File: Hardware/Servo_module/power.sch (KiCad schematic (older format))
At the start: 11 parts, among them P2 CONN_2, P3 CONN_2

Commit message: [HARDWARE][SERVO_MODULE] Schematic
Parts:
- R2: value 1k -> 820
- R3: value 330 -> 220
- R4: value 560 -> 330
- gave numbers to parts that had none: 1
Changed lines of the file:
@@
-EESchema Schematic File Version 2  date Fri 18 Oct 2013 03:55:12 PM CEST
+EESchema Schematic File Version 2
 LIBS:power
 LIBS:device
@@
 LIBS:conn_2_jst
 LIBS:conn_4_jst
+LIBS:sn65hvd232d
 LIBS:serv_module-cache
-EELAYER 24  0
+EELAYER 27 0
 EELAYER END
-$Descr A4 11700 8267
+$Descr A4 11693 8268
+encoding utf-8
 Sheet 2 4
 Title ""
-Date "18 oct 2013"
+Date "25 oct 2013"
 Rev ""
 Comp ""
@@
 	5000 5450 5200 5450
 $Comp
-L LED D?
+L LED D3
 U 1 1 52613CD7
 P 5200 5250
-F 0 "D?" H 5200 5350 50  0000 C CNN
+F 0 "D3" H 5200 5350 50  0000 C CNN
 F 1 "LED" H 5200 5150 50  0000 C CNN
+F 2 "" H 5200 5250 60  0001 C CNN
+F 3 "" H 5200 5250 60  0001 C CNN
 	1    5200 5250
 	0    1    1    0
@@
 P 5200 4750
 F 0 "R4" V 5280 4750 50  0000 C CNN
-F 1 "560" V 5200 4750 50  0000 C CNN
+F 1 "330" V 5200 4750 50  0000 C CNN
+F 2 "" H 5200 4750 60  0001 C CNN
+F 3 "" H 5200 4750 60  0001 C CNN
 	1    5200 4750
 	-1   0    0    1
@@
 F 0 "#PWR?" H 7350 3700 30  0001 C CNN
 F 1 "GND" H 7350 3630 30  0001 C CNN
+F 2 "" H 7350 3700 60  0001 C CNN
+F 3 "" H 7350 3700 60  0001 C CNN
 	1    7350 3700
 	1    0    0    -1
@@
 F 0 "D2" H 7350 3550 50  0000 C CNN
 F 1 "LED" H 7350 3350 50  0000 C CNN
+F 2 "" H 7350 3450 60  0001 C CNN
+F 3 "" H 7350 3450 60  0001 C CNN
 	1    7350 3450
 	0    1    1    0
@@
 P 7050 3250
 F 0 "R3" V 7130 3250 50  0000 C CNN
-F 1 "330" V 7050 3250 50  0000 C CNN
+F 1 "220" V 7050 3250 50  0000 C CNN
+F 2 "" H 7050 3250 60  0001 C CNN
+F 3 "" H 7050 3250 60  0001 C CNN
 	1    7050 3250
 	0    1    1    0
@@
 F 0 "#PWR?" H 4800 2350 30  0001 C CNN
 F 1 "GND" H 4800 2280 30  0001 C CNN
+F 2 "" H 4800 2350 60  0001 C CNN
+F 3 "" H 4800 2350 60  0001 C CNN
 	1    4800 2350
 	1    0    0    -1
@@
 F 0 "D1" H 4950 2600 50  0000 C CNN
 F 1 "LED" H 4950 2400 50  0000 C CNN
+F 2 "" H 4950 2500 60  0001 C CNN
+F 3 "" H 4950 2500 60  0001 C CNN
 	1    4950 2500
 	0    -1   -1   0
@@
 P 4950 3000
 F 0 "R2" V 5030 3000 50  0000 C CNN
-F 1 "1k" V 4950 3000 50  0000 C CNN
+F 1 "820" V 4950 3000 50  0000 C CNN
+F 2 "" H 4950 3000 60  0001 C CNN
+F 3 "" H 4950 3000 60  0001 C CNN
 	1    4950 3000
 	1    0    0    -1
@@
 F 0 "#PWR?" H 5100 5500 30  0001 C CNN
 F 1 "GND" H 5100 5430 30  0001 C CNN
+F 2 "" H 5100 5500 60  0001 C CNN
+F 3 "" H 5100 5500 60  0001 C CNN
 	1    5100 5500
 	1    0    0    -1
@@
 F 0 "P3" V 4550 4600 40  0000 C CNN
 F 1 "CONN_2" V 4650 4600 40  0000 C CNN
+F 2 "" H 4600 4600 60  0001 C CNN
+F 3 "" H 4600 4600 60  0001 C CNN
 	1    4600 4600
 	-1   0    0    -1
@@
 F 0 "P2" V 4450 3350 40  0000 C CNN
 F 1 "CONN_2" V 4550 3350 40  0000 C CNN
+F 2 "" H 4500 3350 60  0001 C CNN
+F 3 "" H 4500 3350 60  0001 C CNN
 	1    4500 3350
 	-1   0    0    -1
@@
 F 0 "U?" H 6300 2900 60  0000 C CNN
 F 1 "AP1117" H 6000 3400 60  0000 C CNN
+F 2 "" H 6050 3250 60  0001 C CNN
+F 3 "" H 6050 3250 60  0001 C CNN
 	1    6050 3250
 	1    0    0    -1
@@
 F 0 "#PWR?" H 6700 3210 30  0001 C CNN
 F 1 "+3.3V" H 6700 3360 30  0000 C CNN
+F 2 "" H 6700 3250 60  0001 C CNN
+F 3 "" H 6700 3250 60  0001 C CNN
 	1    6700 3250
 	1    0    0    -1
@@
 F 0 "22u" H 6750 3600 50  0000 L CNN
 F 1 "CP2" H 6750 3400 50  0000 L CNN
+F 2 "" H 6700 3500 60  0001 C CNN
+F 3 "" H 6700 3500 60  0001 C CNN
 	1    6700 3500
 	1    0    0    -1
@@
 F 0 "10u" H 5450 3600 50  0000 L CNN
 F 1 "CP1" H 5450 3400 50  0000 L CNN
+F 2 "" H 5400 3500 60  0001 C CNN
+F 3 "" H 5400 3500 60  0001 C CNN
 	1    5400 3500
 	1    0    0    -1
@@
 F 0 "#PWR?" H 6050 3850 30  0001 C CNN
 F 1 "GND" H 6050 3780 30  0001 C CNN
+F 2 "" H 6050 3850 60  0001 C CNN
+F 3 "" H 6050 3850 60  0001 C CNN
 	1    6050 3850
 	1    0    0    -1

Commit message: [HARDWARE][SERVO_MODULE] Schematic
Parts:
- CP1: renamed from 10u; value CP1 -> 10u
- CP2: renamed from 22u; value CP2 -> 22u
- gave numbers to parts that had none: 1
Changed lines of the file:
@@
 $EndComp
 $Comp
-L GND #PWR?
+L GND #PWR01
 U 1 1 52613C2B
 P 7350 3700
-F 0 "#PWR?" H 7350 3700 30  0001 C CNN
+F 0 "#PWR01" H 7350 3700 30  0001 C CNN
 F 1 "GND" H 7350 3630 30  0001 C CNN
 F 2 "" H 7350 3700 60  0001 C CNN
@@
 $EndComp
 $Comp
-L GND #PWR?
+L GND #PWR02
 U 1 1 52613B24
 P 4800 2350
-F 0 "#PWR?" H 4800 2350 30  0001 C CNN
+F 0 "#PWR02" H 4800 2350 30  0001 C CNN
 F 1 "GND" H 4800 2280 30  0001 C CNN
 F 2 "" H 4800 2350 60  0001 C CNN
@@
 SERVO_POWER
 $Comp
-L GND #PWR?
+L GND #PWR03
 U 1 1 526136B4
 P 5100 5500
-F 0 "#PWR?" H 5100 5500 30  0001 C CNN
+F 0 "#PWR03" H 5100 5500 30  0001 C CNN
 F 1 "GND" H 5100 5430 30  0001 C CNN
 F 2 "" H 5100 5500 60  0001 C CNN
@@
 $EndComp
 $Comp
-L AP1117 U?
+L AP1117 U2
 U 1 1 52613406
 P 6050 3250
-F 0 "U?" H 6300 2900 60  0000 C CNN
+F 0 "U2" H 6300 2900 60  0000 C CNN
 F 1 "AP1117" H 6000 3400 60  0000 C CNN
 F 2 "" H 6050 3250 60  0001 C CNN
@@
 $EndComp
 $Comp
-L +3.3V #PWR?
+L +3.3V #PWR04
 U 1 1 526135E7
 P 6700 3250
-F 0 "#PWR?" H 6700 3210 30  0001 C CNN
+F 0 "#PWR04" H 6700 3210 30  0001 C CNN
 F 1 "+3.3V" H 6700 3360 30  0000 C CNN
 F 2 "" H 6700 3250 60  0001 C CNN
@@
 $EndComp
 $Comp
-L CP 22u
+L CP CP2
 U 1 1 526135C0
 P 6700 3500
-F 0 "22u" H 6750 3600 50  0000 L CNN
-F 1 "CP2" H 6750 3400 50  0000 L CNN
+F 0 "CP2" H 6750 3600 50  0000 L CNN
+F 1 "22u" H 6750 3400 50  0000 L CNN
 F 2 "" H 6700 3500 60  0001 C CNN
 F 3 "" H 6700 3500 60  0001 C CNN
@@
 $EndComp
 $Comp
-L CP 10u
+L CP CP1
 U 1 1 526135BB
 P 5400 3500
-F 0 "10u" H 5450 3600 50  0000 L CNN
-F 1 "CP1" H 5450 3400 50  0000 L CNN
+F 0 "CP1" H 5450 3600 50  0000 L CNN
+F 1 "10u" H 5450 3400 50  0000 L CNN
 F 2 "" H 5400 3500 60  0001 C CNN
 F 3 "" H 5400 3500 60  0001 C CNN
@@
 $EndComp
 $Comp
-L GND #PWR?
+L GND #PWR05
 U 1 1 52613414
 P 6050 3850
-F 0 "#PWR?" H 6050 3850 30  0001 C CNN
+F 0 "#PWR05" H 6050 3850 30  0001 C CNN
 F 1 "GND" H 6050 3780 30  0001 C CNN
 F 2 "" H 6050 3850 60  0001 C CNN

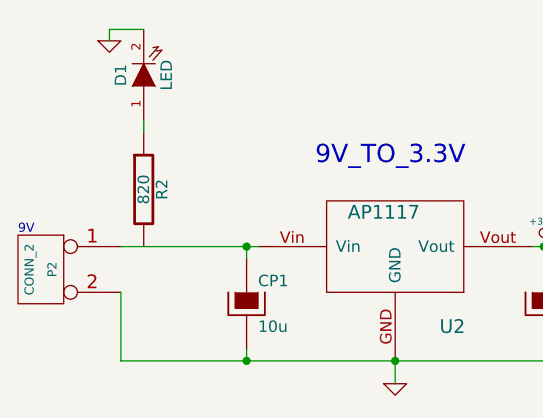
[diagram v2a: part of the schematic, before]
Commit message: [HARDWARE][SERVO_MODULE] Update schemating & routing
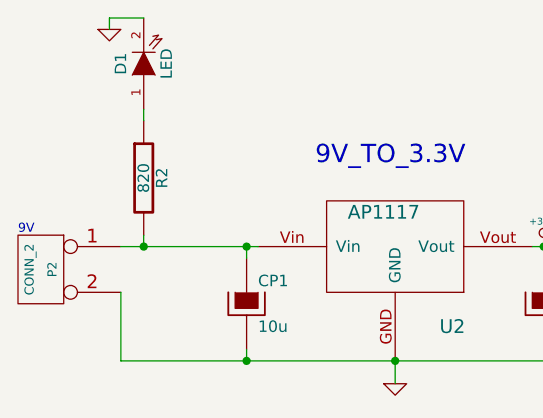
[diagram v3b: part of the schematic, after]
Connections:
- net at CP1.1, P2.1 (P1), U2.Vin: now also R2.2
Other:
- moved on the sheet: D1, R2
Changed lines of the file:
@@
 LIBS:contrib
 LIBS:valves
-LIBS:stm32f103c4
 LIBS:ap1117
 LIBS:conn_2_jst
 LIBS:conn_4_jst
 LIBS:sn65hvd232d
+LIBS:stm32f103c4
 LIBS:serv_module-cache
 EELAYER 27 0
@@
 $Descr A4 11693 8268
 encoding utf-8
-Sheet 2 4
+Sheet 4 4
 Title ""
 Date "25 oct 2013"
@@
 	5200 5000 5200 5050
 Wire Wire Line
-	4800 2350 4800 2300
+	4800 2300 4800 2250
 Wire Wire Line
 	7300 3250 7350 3250
 Wire Wire Line
-	4950 2700 4950 2750
+	4950 2650 4950 2700
 Connection ~ 5400 3250
 Wire Wire Line
@@
 	7350 3650 7350 3700
 Wire Wire Line
-	4800 2300 4950 2300
+	4800 2250 4950 2250
 Wire Wire Line
 	5250 4500 4950 4500
@@
 $EndComp
 $Comp
-L GND #PWR01
+L GND #PWR050
 U 1 1 52613C2B
 P 7350 3700
-F 0 "#PWR01" H 7350 3700 30  0001 C CNN
+F 0 "#PWR050" H 7350 3700 30  0001 C CNN
 F 1 "GND" H 7350 3630 30  0001 C CNN
 F 2 "" H 7350 3700 60  0001 C CNN
@@
 $EndComp
 $Comp
-L GND #PWR02
+L GND #PWR051
 U 1 1 52613B24
-P 4800 2350
-F 0 "#PWR02" H 4800 2350 30  0001 C CNN
-F 1 "GND" H 4800 2280 30  0001 C CNN
-F 2 "" H 4800 2350 60  0001 C CNN
-F 3 "" H 4800 2350 60  0001 C CNN
-	1    4800 2350
+P 4800 2300
+F 0 "#PWR051" H 4800 2300 30  0001 C CNN
+F 1 "GND" H 4800 2230 30  0001 C CNN
+F 2 "" H 4800 2300 60  0001 C CNN
+F 3 "" H 4800 2300 60  0001 C CNN
+	1    4800 2300
 	1    0    0    -1
 $EndComp
@@
 L LED D1
 U 1 1 52613B17
-P 4950 2500
-F 0 "D1" H 4950 2600 50  0000 C CNN
-F 1 "LED" H 4950 2400 50  0000 C CNN
-F 2 "" H 4950 2500 60  0001 C CNN
-F 3 "" H 4950 2500 60  0001 C CNN
-	1    4950 2500
+P 4950 2450
+F 0 "D1" H 4950 2550 50  0000 C CNN
+F 1 "LED" H 4950 2350 50  0000 C CNN
+F 2 "" H 4950 2450 60  0001 C CNN
+F 3 "" H 4950 2450 60  0001 C CNN
+	1    4950 2450
 	0    -1   -1   0
 $EndComp
@@
 L R R2
 U 1 1 52613B05
-P 4950 3000
-F 0 "R2" V 5030 3000 50  0000 C CNN
-F 1 "820" V 4950 3000 50  0000 C CNN
-F 2 "" H 4950 3000 60  0001 C CNN
-F 3 "" H 4950 3000 60  0001 C CNN
-	1    4950 3000
+P 4950 2950
+F 0 "R2" V 5030 2950 50  0000 C CNN
+F 1 "820" V 4950 2950 50  0000 C CNN
+F 2 "" H 4950 2950 60  0001 C CNN
+F 3 "" H 4950 2950 60  0001 C CNN
+	1    4950 2950
 	1    0    0    -1
 $EndComp
@@
 SERVO_POWER
 $Comp
-L GND #PWR03
+L GND #PWR052
 U 1 1 526136B4
 P 5100 5500
-F 0 "#PWR03" H 5100 5500 30  0001 C CNN
+F 0 "#PWR052" H 5100 5500 30  0001 C CNN
 F 1 "GND" H 5100 5430 30  0001 C CNN
 F 2 "" H 5100 5500 60  0001 C CNN
@@
 $EndComp
 $Comp
-L +3.3V #PWR04
+L +3.3V #PWR053
 U 1 1 526135E7
 P 6700 3250
-F 0 "#PWR04" H 6700 3210 30  0001 C CNN
+F 0 "#PWR053" H 6700 3210 30  0001 C CNN
 F 1 "+3.3V" H 6700 3360 30  0000 C CNN
 F 2 "" H 6700 3250 60  0001 C CNN
@@
 $EndComp
 $Comp
-L GND #PWR05
+L GND #PWR054
 U 1 1 52613414
 P 6050 3850
-F 0 "#PWR05" H 6050 3850 30  0001 C CNN
+F 0 "#PWR054" H 6050 3850 30  0001 C CNN
 F 1 "GND" H 6050 3780 30  0001 C CNN
 F 2 "" H 6050 3850 60  0001 C CNN
@@
 	1    0    0    -1
 $EndComp
+Wire Wire Line
+	4950 3200 4950 3250
+Connection ~ 4950 3250
 $EndSCHEMATC
